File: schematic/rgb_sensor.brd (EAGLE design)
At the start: 63.2 x 81.3 mm, 6 parts, among them IC2 MEGA8-P

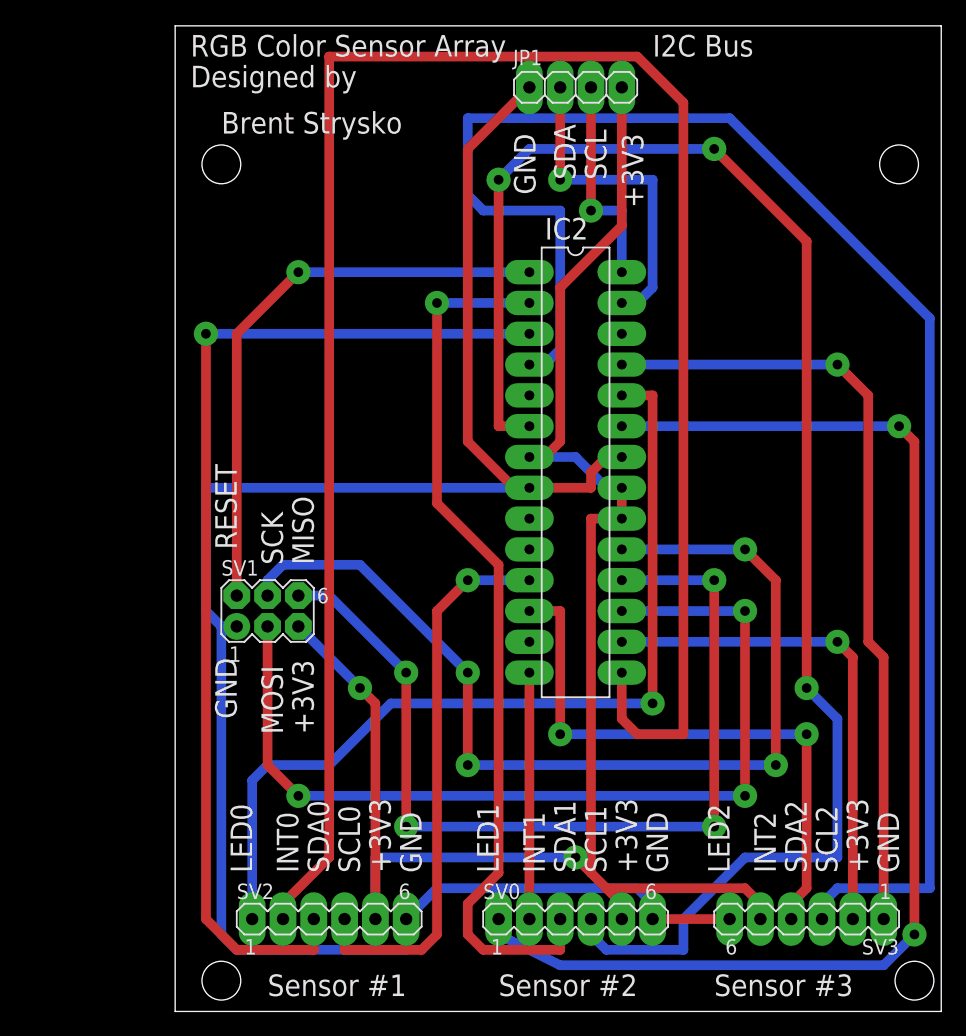
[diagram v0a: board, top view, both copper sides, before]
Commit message: Redesigned schematic and board.  Added decoupling capacitors, pullup resistor on reset, and shrunk board size
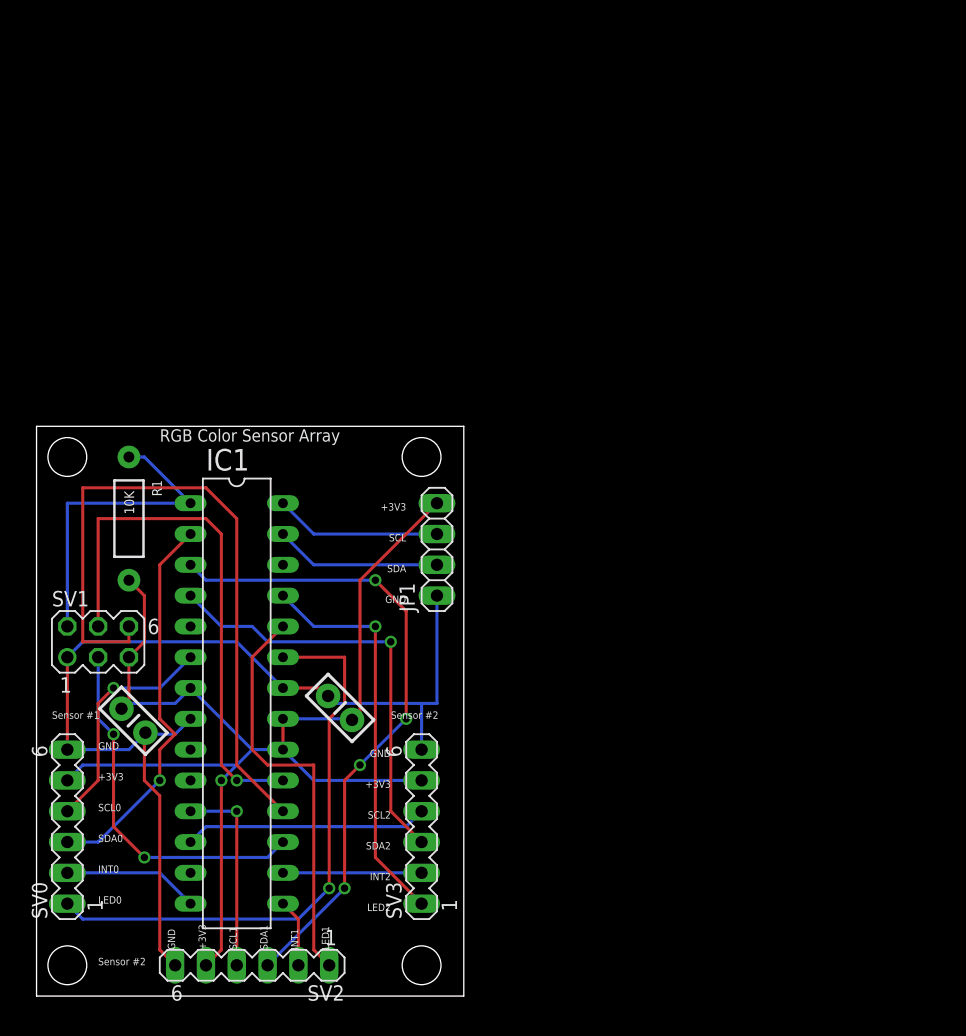
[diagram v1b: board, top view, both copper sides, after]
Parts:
- removed IC2: MEGA8-P, atmel:DIL28-3
- added C1, C2: 1uF, SparkFun-Passives:CAP-PTH-SMALL-KIT
- added IC1: MEGA8-P, atmel:DIL28-3
- added R1: 10K, SparkFun-Passives:AXIAL-0.4
- SV0: value (none) -> RGB Color Sensor #0
- SV2: value (none) -> RGB Color Sensor #1
- SV3: value (none) -> RGB Color Sensor #3
- moved SV0 42.6 mm to (2.54, 14.0), turned to 90 degrees
- moved JP1 39.8 mm to (33.0, 36.8), turned to 90 degrees
- moved SV3 32.7 mm to (31.8, 14.0), turned to 90 degrees
- moved SV1 14.2 mm to (5.08, 29.2)
- moved SV2 7.41 mm to (17.8, 2.54), turned to 180 degrees
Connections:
- net +3V3: now also C1.1, C2.1, IC1.20, IC1.21, IC1.7, R1.P$2; no longer IC2.20, IC2.21, IC2.7
- net BBB_SCL: now also IC1.28; no longer IC2.28
- net BBB_SDA: now also IC1.27; no longer IC2.27
- net GND: now also C1.2, C2.2, IC1.22, IC1.8; no longer IC2.22, IC2.8
- net INT0: now also IC1.14; no longer IC2.14
- net INT1: now also IC1.15; no longer IC2.15
- net INT2: now also IC1.16; no longer IC2.16
- net LED0: now also IC1.23; no longer IC2.23
- net LED1: now also IC1.24; no longer IC2.24
- net LED2: now also IC1.25; no longer IC2.25
- net MISO: now also IC1.18; no longer IC2.18
- net MOSI: now also IC1.17; no longer IC2.17
- net RESET: now also IC1.1, R1.P$1; no longer IC2.1
- net SCK: now also IC1.19; no longer IC2.19
- net SCL0: now also IC1.6; no longer IC2.6
- net SCL1: now also IC1.11; no longer IC2.11
- net SCL2: now also IC1.12; no longer IC2.12
- net SDA0: now also IC1.2; no longer IC2.2
- net SDA1: now also IC1.3; no longer IC2.3
- net SDA2: now also IC1.4; no longer IC2.4
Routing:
- net INT1: track 165.0 -> 5.61 mm
- net SCL0: track 131.1 -> 19.1 mm, vias 3 -> 1
- net SDA2: track 131.6 -> 35.7 mm, vias 0 -> 1
- net GND: track 160.5 -> 85.8 mm
- net LED0: track 102.5 -> 47.8 mm, vias 2 -> 1
- net MOSI: track 77.3 -> 30.0 mm, vias 3 -> 2
- net +3V3: track 146.8 -> 103.7 mm, vias 2 -> 1
- net SDA0: track 73.5 -> 32.1 mm
- net LED1: track 75.0 -> 33.9 mm, vias 1 -> 0
- net SCK: track 84.0 -> 44.2 mm, vias 4 -> 1
- net SDA1: track 87.4 -> 53.3 mm, vias 1 -> 4
- net LED2: track 65.1 -> 33.1 mm
- net INT2: track 41.2 -> 11.4 mm, vias 1 -> 0
- net SCL1: track 46.0 -> 16.5 mm
- net SCL2: track 48.8 -> 20.1 mm, vias 2 -> 0
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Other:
- board size 63.2 x 81.3 mm -> 35.2 x 47 mm
- board text removed: "Brent Strysko"
- board text removed: "Designed by"
- board text removed: "I2C Bus"
- board text removed: "MISO"
- board text removed: "MOSI"
- board text removed: "RESET"
- board text removed: "SCK"
- board text removed: "Sensor #3"
